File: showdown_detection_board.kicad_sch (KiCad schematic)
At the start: 30 parts, among them J1 Conn_01x04_Pin, J2 USB4155-03-C_REVA, SW1 SW_SPDT, U1 AMS1117-3.3, U3 STM32F103C8T6, U5 ${SIM.PARAMS}, Y1 16MHz

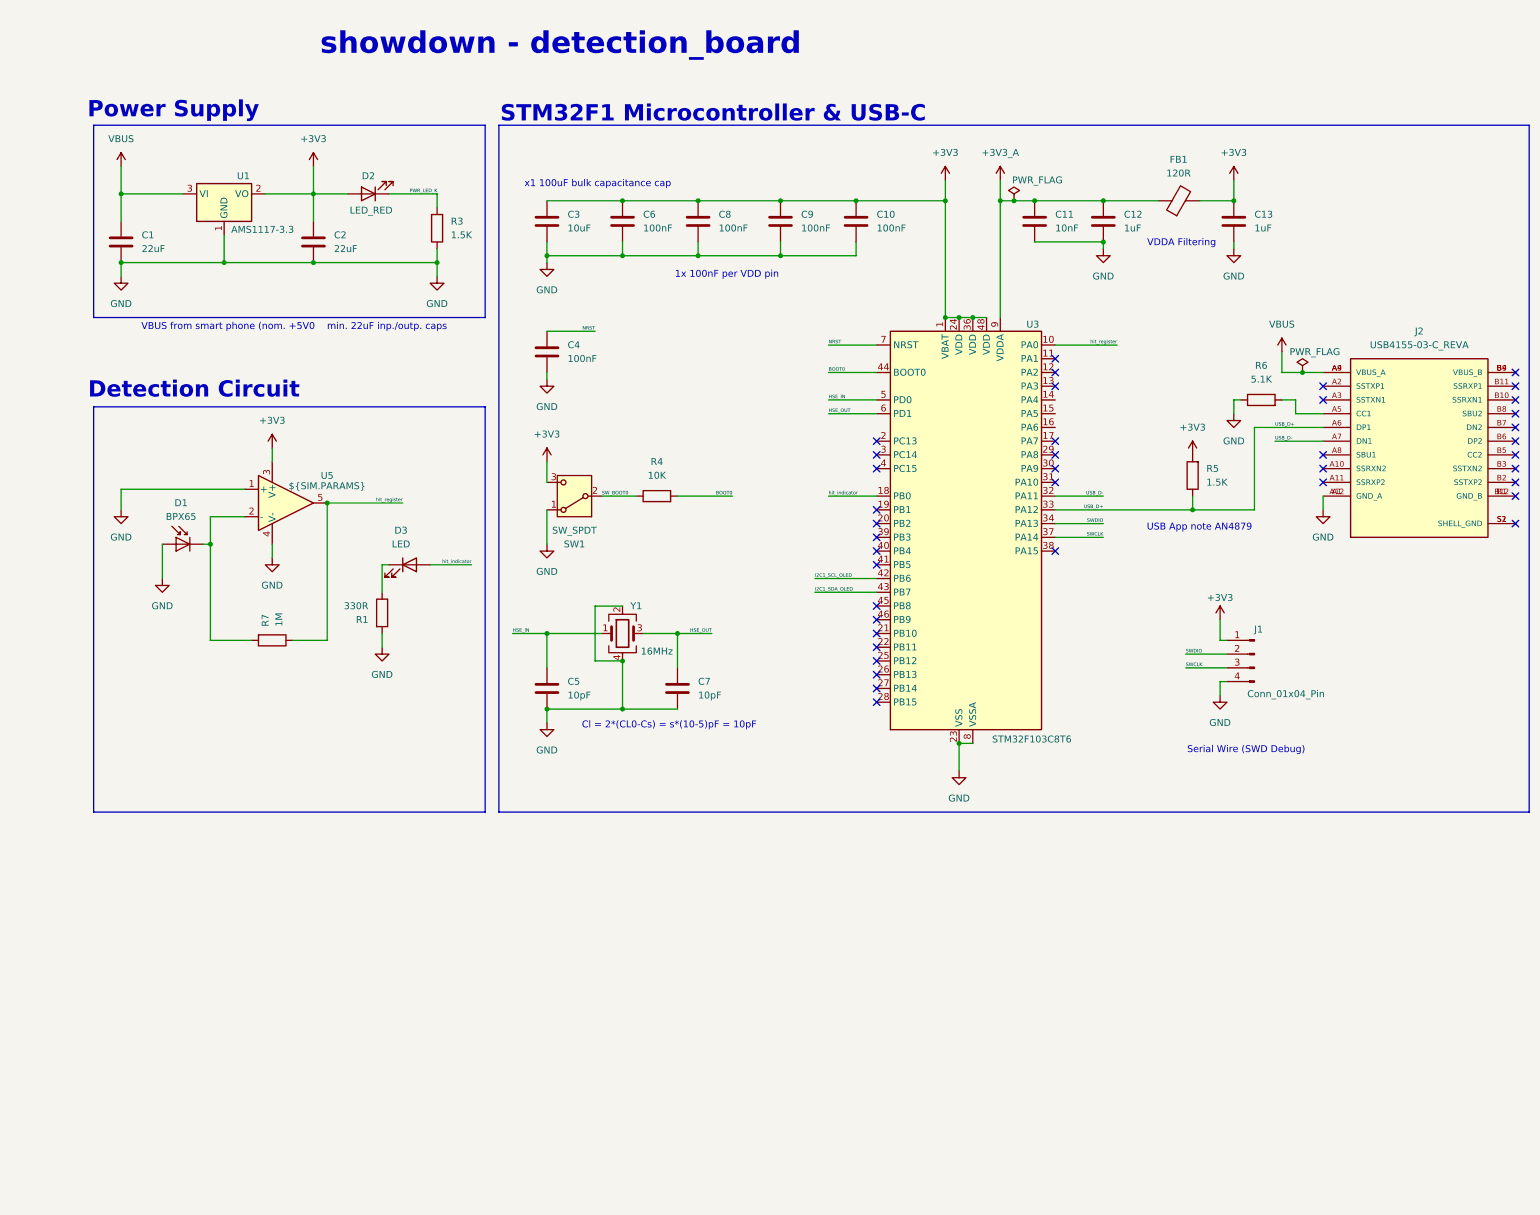
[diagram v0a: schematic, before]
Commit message: most of schematic is complete
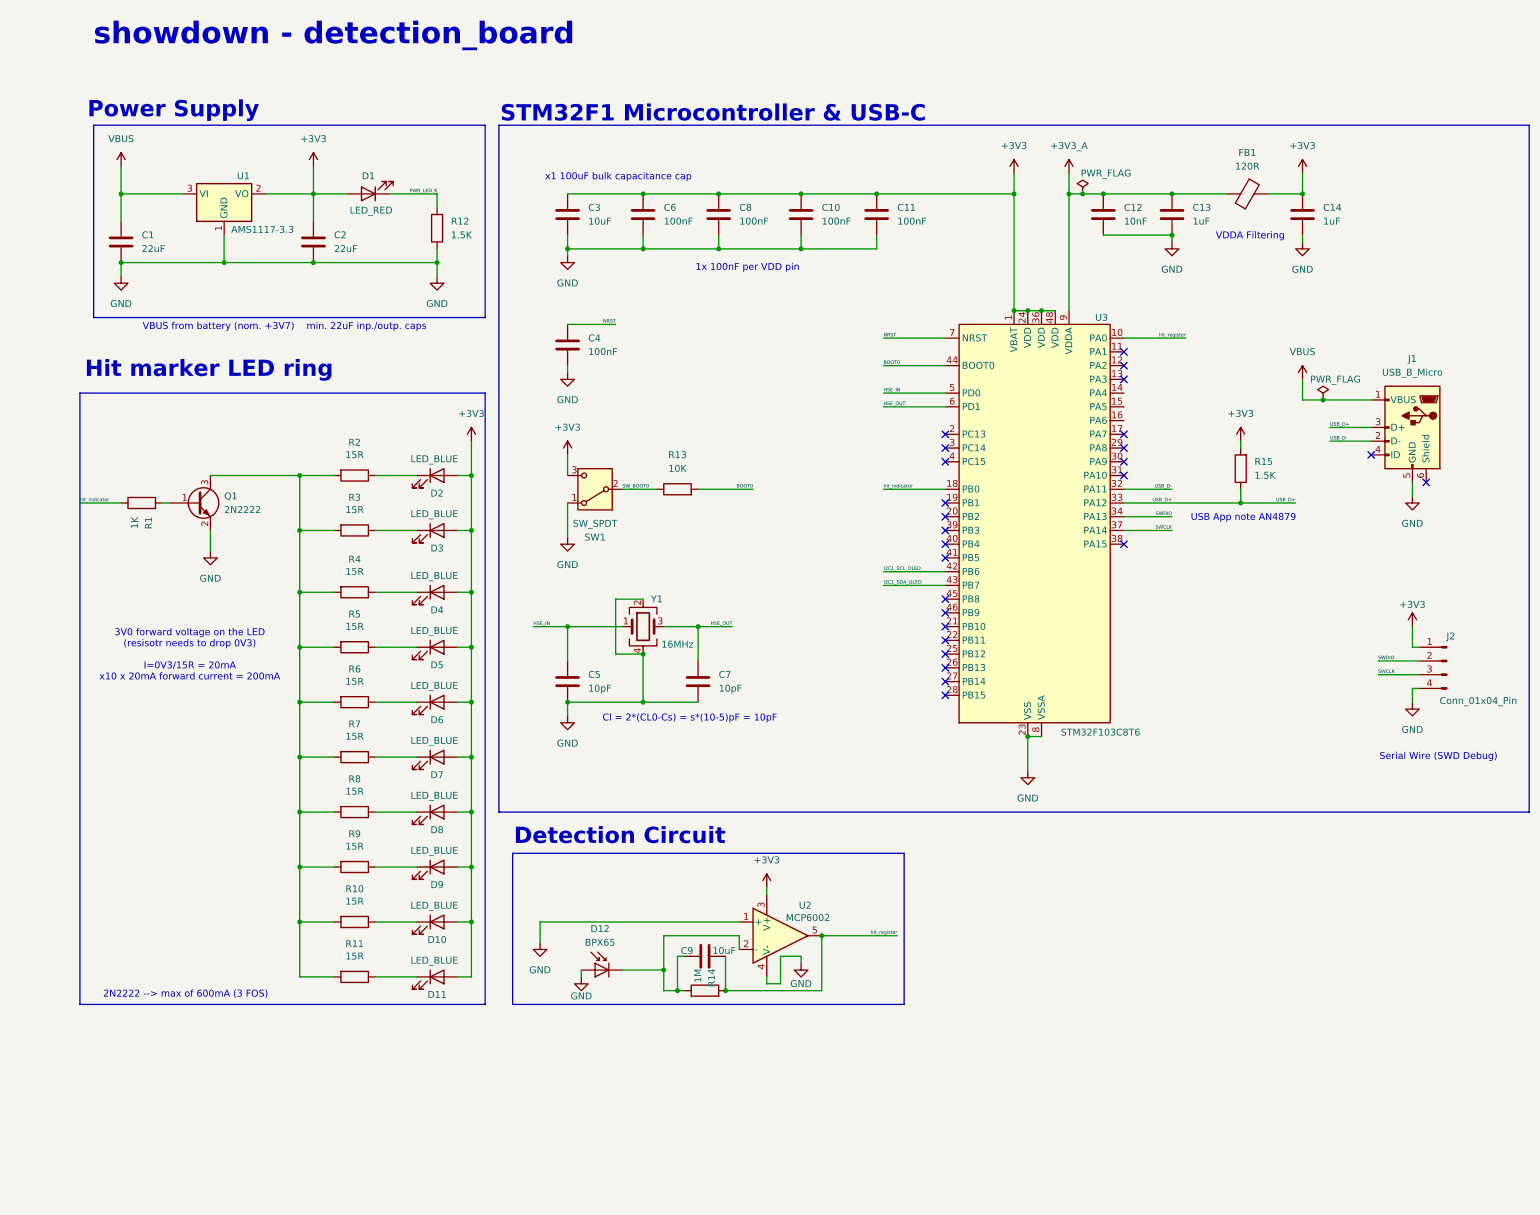
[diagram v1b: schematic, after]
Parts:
- removed J2: USB4155-03-C_REVA, USB4155-03-C_REVA:GCT_USB4155-03-C_REVA, symbol USB4155-03-C:USB4155-03-C_REVA
- added C9: 10uF, Capacitor_SMD:C_0603_1608Metric, symbol Device:C
- added D10, D11, D2, D4, D5, D6, D7, D8, D9: LED_BLUE, LED_SMD:LED_0805_2012Metric, symbol Device:LED
- added J1: USB_B_Micro, Connector_USB:USB_Micro-AB_Molex_47590-0001, symbol Connector:USB_B_Micro
- added Q1: 2N2222, Package_TO_SOT_THT:TO-92, symbol Device:Q_NPN_BEC
- added R10, R11, R2, R3, R4, R5, R7, R8, R9: 15R, Resistor_SMD:R_0603_1608Metric, symbol Device:R
- D3: value LED -> LED_BLUE; footprint (none) -> LED_SMD:LED_0805_2012Metric
- R1: value 330R -> 1K
- R6: value 5.1K -> 15R
- SW1: footprint Button_Switch_THT:SW_E-Switch_EG1271_SPDT -> Button_Switch_THT:SW_Slide-03_Wuerth-WS-SLTV_10x2.5x6.4_P2.54mm
- U2: renamed from U5; value ${SIM.PARAMS} -> MCP6002; footprint (none) -> Package_DFN_QFN:TDFN-8-1EP_3x2mm_P0.5mm_EP1.3x1.4mm
- renumbered C9 to C10, C10 to C11, C11 to C12, C12 to C13, C13 to C14, D2 to D1, D1 to D12, J1 to J2, R3 to R12, R4 to R13, R7 to R14, R5 to R15
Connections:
- net +3V3: now also D3.2 (A), D10.2 (A), D11.2 (A), D2.2 (A), D4.2 (A), D5.2 (A), D6.2 (A), D7.2 (A), D8.2 (A), D9.2 (A)
- net GND: now also J1.5 (GND), Q1.2 (E); no longer R1.2, R6.1
- net USB_D+: now also J1.3 (D+)
- net USB_D-: now also J1.2 (D-)
- net VBUS: now also J1.1 (VBUS)
- net hit_indicator: now also R1.1; no longer D3.2 (A)
- net hit_register: now also R14.2, C9.1; no longer R14.1
- net at D12.1 (K), U2.2 (-): now also R14.1, C9.2; no longer R14.2
- net at R6.2: now also Q1.3 (C), R10.2, R11.2, R2.2, R3.2, R4.2, R5.2, R7.2, R8.2, R9.2
- net at D3.1 (K): now also R3.1; no longer R1.1
- new net: D6.1 (K), R6.1
- new net: D9.1 (K), R9.1
- new net: D11.1 (K), R11.1
- new net: D10.1 (K), R10.1
- new net: D8.1 (K), R8.1
- new net: D4.1 (K), R4.1
- new net: D2.1 (K), R2.1
- new net: D7.1 (K), R7.1
- new net: Q1.1 (B), R1.2
- new net: D5.1 (K), R5.1
- no-connect marks 40 -> 26
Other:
- note added: "2N2222 --> max of 600mA (3 FOS)"
- note added: "3V0 forward voltage on the LED (resisotr needs to drop 0V3) I=0V3/15R = 20mA x10 x 20mA forward current = 200mA"
- note added: "Hit marker LED ring"
- note added: "VBUS from battery (nom. +3V7) min. 22uF inp./outp. caps"
- note removed: "VBUS from smart phone (nom. +5V0 min. 22uF inp./outp. caps"
- moved on the sheet: C10, C11, C12, C13, C14, C3, C4, C5, C6, C7, C8, D12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

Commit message: started working on battery cir.
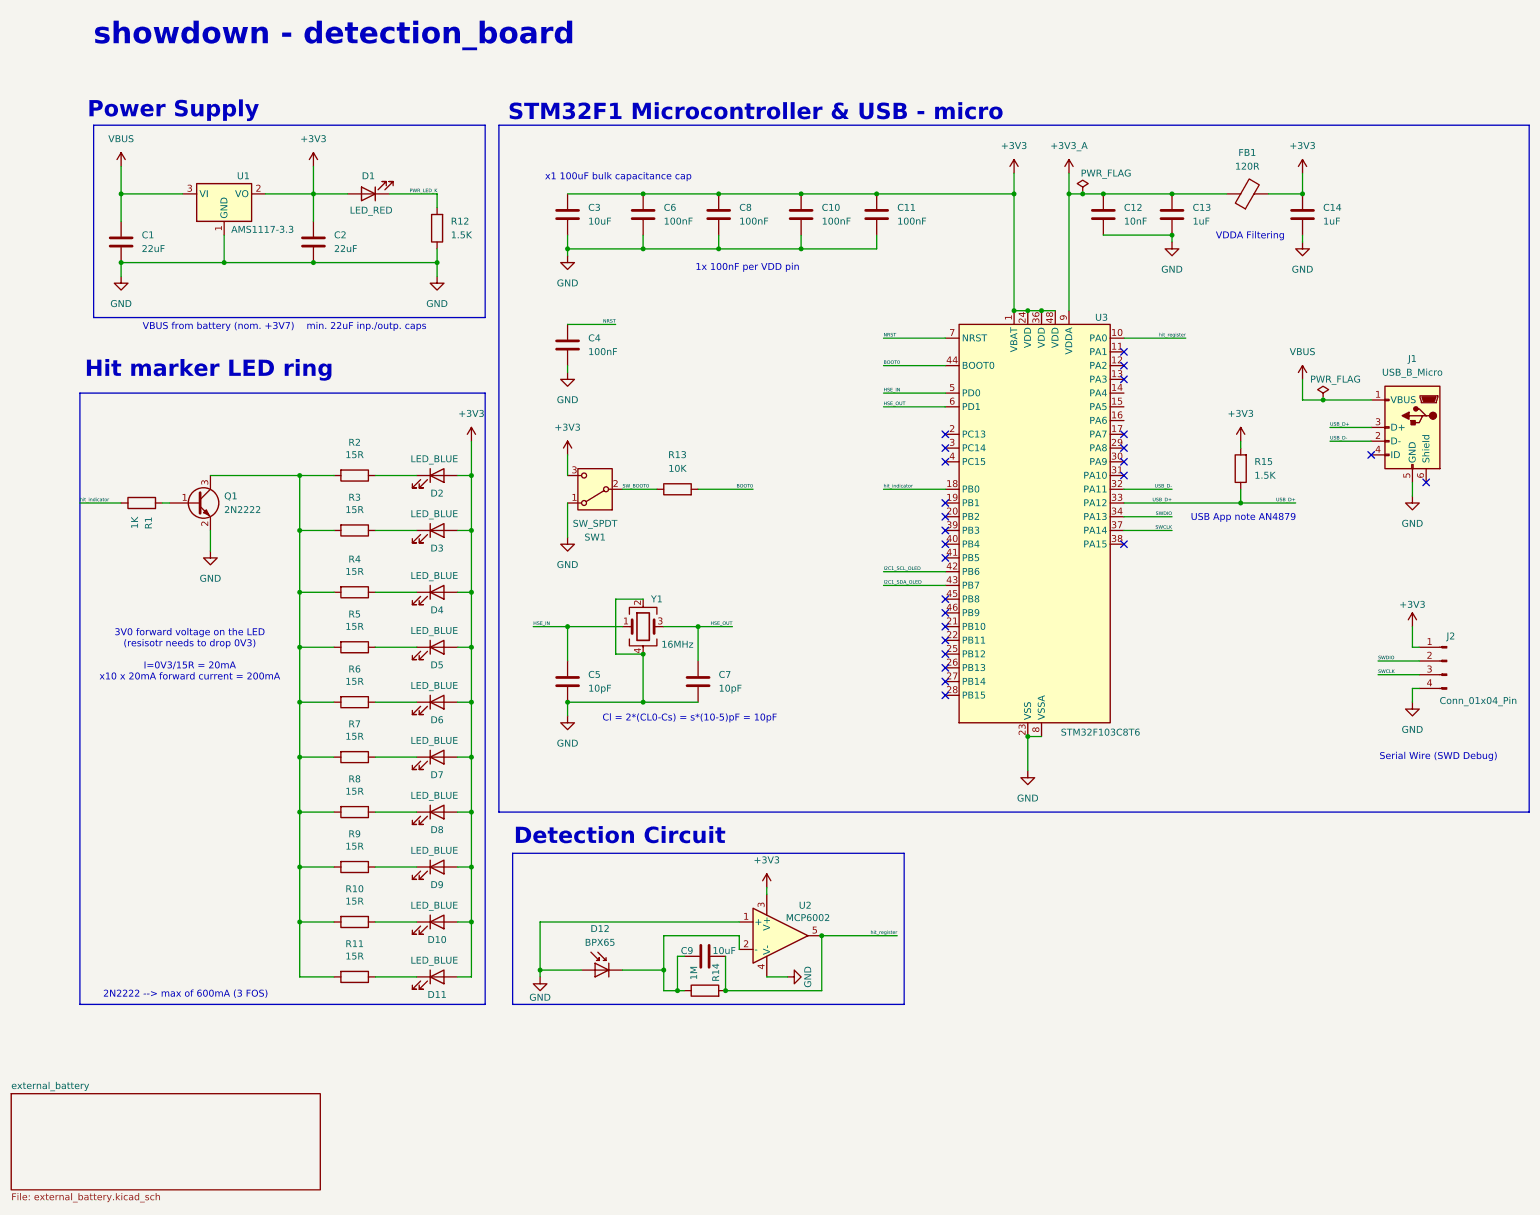
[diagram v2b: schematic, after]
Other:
- added sheet external_battery (external_battery.kicad_sch)
- note added: "STM32F1 Microcontroller & USB - micro"
- note removed: "STM32F1 Microcontroller & USB-C"
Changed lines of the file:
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@@
 	)
 	(junction
+		(at 97.79 190.5)
+		(diameter 0)
+		(color 0 0 0 0)
+	)
+	(junction
 		(at 132.08 194.31)
 		(diameter 0)
@@
 	(wire
 		(pts
+			(xy 53.34 151.13) (xy 53.34 161.29)
+		)
+		(stroke
+			(width 0)
+			(type default)
+		)
+	)
+	(wire
+		(pts
 			(xy 146.05 57.15) (xy 160.02 57.15)
 		)
@@
 	(wire
 		(pts
-			(xy 161.29 119.38) (xy 172.72 119.38)
+			(xy 97.79 191.77) (xy 97.79 190.5)
 		)
 		(stroke
@@
 	(wire
 		(pts
-			(xy 142.24 187.96) (xy 146.05 187.96)
+			(xy 161.29 119.38) (xy 172.72 119.38)
 		)
 		(stroke
@@
 	(wire
 		(pts
-			(xy 146.05 187.96) (xy 146.05 189.23)
-		)
-		(stroke
-			(width 0)
-			(type default)
-		)
-	)
-	(wire
-		(pts
-			(xy 97.79 181.61) (xy 97.79 185.42)
+			(xy 97.79 181.61) (xy 97.79 190.5)
 		)
 		(stroke
@@
 	(wire
 		(pts
-			(xy 139.7 193.04) (xy 139.7 191.77)
+			(xy 116.84 140.97) (xy 116.84 132.08)
 		)
 		(stroke
@@
 	(wire
 		(pts
-			(xy 116.84 140.97) (xy 116.84 132.08)
+			(xy 185.42 68.58) (xy 187.96 68.58)
 		)
 		(stroke
@@
 	(wire
 		(pts
-			(xy 185.42 68.58) (xy 187.96 68.58)
+			(xy 97.79 190.5) (xy 105.41 190.5)
 		)
 		(stroke
@@
 	(wire
 		(pts
-			(xy 142.24 193.04) (xy 142.24 187.96)
-		)
-		(stroke
-			(width 0)
-			(type default)
-		)
-	)
-	(wire
-		(pts
 			(xy 74.93 109.22) (xy 67.31 109.22)
 		)
@@
 	(wire
 		(pts
-			(xy 53.34 151.13) (xy 53.34 161.29)
-		)
-		(stroke
-			(width 0)
-			(type default)
-		)
-	)
-	(wire
-		(pts
 			(xy 20.32 59.69) (xy 20.32 62.23)
 		)
@@
 	(wire
 		(pts
-			(xy 139.7 193.04) (xy 142.24 193.04)
-		)
-		(stroke
-			(width 0)
-			(type default)
-		)
-	)
-	(wire
-		(pts
 			(xy 82.55 181.61) (xy 85.09 181.61)
 		)
@@
 	(wire
 		(pts
-			(xy 105.41 190.5) (xy 105.41 191.77)
-		)
-		(stroke
-			(width 0)
-			(type default)
-		)
-	)
-	(wire
-		(pts
 			(xy 161.29 101.6) (xy 172.72 101.6)
 		)
@@
 	(wire
 		(pts
+			(xy 139.7 191.77) (xy 143.51 191.77)
+		)
+		(stroke
+			(width 0)
+			(type default)
+		)
+	)
+	(wire
+		(pts
 			(xy 85.09 109.22) (xy 85.09 99.06)
 		)
@@
 		)
 	)
-	(text "STM32F1 Microcontroller & USB-C\n"
+	(text "STM32F1 Microcontroller & USB - micro"
 		(exclude_from_sim no)
-		(at 129.794 32.258 0)
+		(at 137.668 32.004 0)
 		(effects
 			(font
@@
 	(symbol
 		(lib_id "power:GND")
-		(at 97.79 185.42 0)
+		(at 97.79 191.77 0)
 		(mirror y)
 		(unit 1)
@@
 		(on_board yes)
 		(dnp no)
-		(fields_autoplaced yes)
 		(property "Reference" "#PWR07"
-			(at 97.79 191.77 0)
+			(at 97.79 198.12 0)
 			(effects
 				(font
@@
 		)
 		(property "Value" "GND"
-			(at 97.79 190.5 0)
+			(at 97.79 195.58 0)
 			(effects
 				(font
@@
 		)
 		(property "Footprint" ""
-			(at 97.79 185.42 0)
+			(at 97.79 191.77 0)
 			(effects
 				(font
@@
 		)
 		(property "Datasheet" ""
-			(at 97.79 185.42 0)
+			(at 97.79 191.77 0)
 			(effects
 				(font
@@
 		)
 		(property "Description" "Power symbol creates a global label with name \"GND\" , ground"
-			(at 97.79 185.42 0)
+			(at 97.79 191.77 0)
 			(effects
 				(font
@@
 	)
 	(symbol
-		(lib_id "power:GND")
-		(at 105.41 191.77 0)
-		(mirror y)
-		(unit 1)
-		(exclude_from_sim no)
-		(in_bom yes)
-		(on_board yes)
-		(dnp no)
-		(property "Reference" "#PWR013"
-			(at 105.41 198.12 0)
-			(effects
-				(font
-					(size 1.27 1.27)
-				)
-				(hide yes)
-			)
-		)
-		(property "Value" "GND"
-			(at 105.41 195.326 0)
-			(effects
-				(font
-					(size 1.27 1.27)
-				)
-			)
-		)
-		(property "Footprint" ""
-			(at 105.41 191.77 0)
-			(effects
-				(font
-					(size 1.27 1.27)
-				)
-				(hide yes)
-			)
-		)
-		(property "Datasheet" ""
-			(at 105.41 191.77 0)
-			(effects
-				(font
-					(size 1.27 1.27)
-				)
-				(hide yes)
-			)
-		)
-		(property "Description" "Power symbol creates a global label with name \"GND\" , ground"
-			(at 105.41 191.77 0)
-			(effects
-				(font
-					(size 1.27 1.27)
-				)
-				(hide yes)
-			)
-		)
-		(pin "1"
-		)
-		(instances
-			(project "showdown"
-				(path "/b2914e51-1eb1-4e40-b847-9ce56891b95a"
-					(reference "#PWR013")
-					(unit 1)
-				)
-			)
-		)
-	)
-	(symbol
 		(lib_id "power:+3.3V")
 		(at 85.09 92.71 0)
@@
 	(symbol
 		(lib_id "power:GND")
-		(at 146.05 189.23 0)
-		(mirror y)
+		(at 143.51 191.77 90)
+		(mirror x)
 		(unit 1)
 		(exclude_from_sim no)
@@
 		(dnp no)
 		(property "Reference" "#PWR015"
-			(at 146.05 195.58 0)
+			(at 149.86 191.77 0)
 			(effects
 				(font
@@
 		)
 		(property "Value" "GND"
-			(at 146.05 193.04 0)
+			(at 147.32 191.77 0)
 			(effects
 				(font
@@
 		)
 		(property "Footprint" ""
-			(at 146.05 189.23 0)
+			(at 143.51 191.77 0)
 			(effects
 				(font
@@
 		)
 		(property "Datasheet" ""
-			(at 146.05 189.23 0)
+			(at 143.51 191.77 0)
 			(effects
 				(font
@@
 		)
 		(property "Description" "Power symbol creates a global label with name \"GND\" , ground"
-			(at 146.05 189.23 0)
+			(at 143.51 191.77 0)
 			(effects
 				(font
@@
 		(dnp no)
 		(property "Reference" "R14"
-			(at 129.54 190.246 0)
+			(at 130.302 189.23 0)
 			(effects
 				(font
@@
 		)
 		(property "Value" "1M"
-			(at 127 190.246 0)
+			(at 126.238 189.738 0)
 			(effects
 				(font
@@
 				)
 			)
+		)
+	)
+	(sheet
+		(at 0 213.36)
+		(size 57.15 17.78)
+		(fields_autoplaced yes)
+		(stroke
+			(width 0.1524)
+			(type solid)
+		)
+		(fill
+			(color 0 0 0 0.0000)
+		)
+		(property "Sheetname" "external_battery"
+			(at 0 212.6484 0)
+			(effects
+				(font
+					(size 1.27 1.27)
+				)
+				(justify left bottom)
+			)
+		)
+		(property "Sheetfile" "external_battery.kicad_sch"
+			(at 0 231.7246 0)
+			(effects
+				(font
+					(size 1.27 1.27)
+				)
+				(justify left top)
+			)
+		)
+		(instances
+			(project "showdown_detection_board"
+				(path "/b2914e51-1eb1-4e40-b847-9ce56891b95a"
+					(page "2")
+				)
+			)
